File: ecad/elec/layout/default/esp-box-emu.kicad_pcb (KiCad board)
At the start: 2 copper layers, 225.7 x 100.8 mm, 0 parts

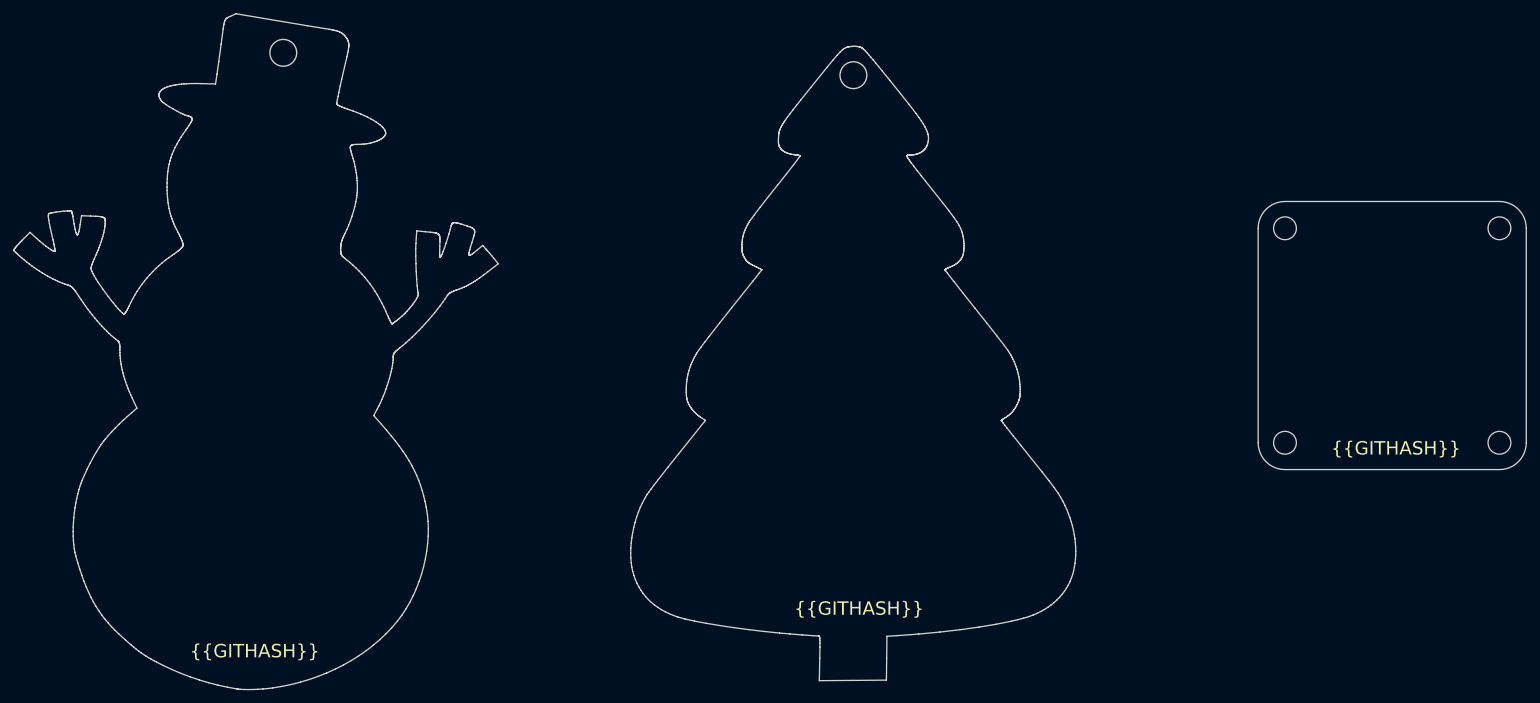
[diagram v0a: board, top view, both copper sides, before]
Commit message: wip: fleshing out ecad in atopile for fun
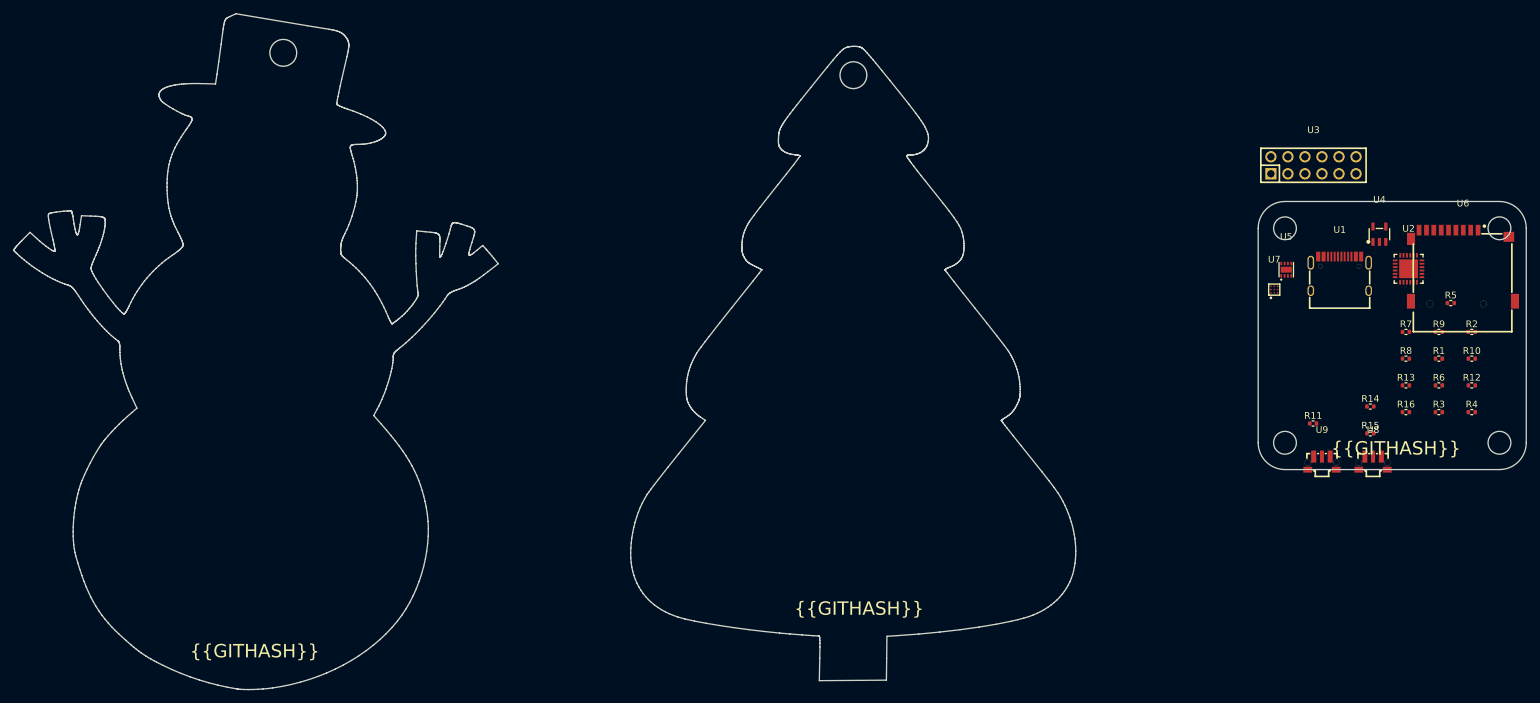
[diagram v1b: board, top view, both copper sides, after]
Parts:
- added R1: 62.5mW Thick Film Resistors ±100ppm/℃ ±1% 5.1kΩ 0402 Chip R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, lib:R0402, F.Cu at (248.6, 101.2)
- added R10: 62.5mW Thick Film Resistors ±100ppm/℃ ±1% 10kΩ 0402 Chip Re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, lib:R0402, F.Cu at (253.5, 101.2)
- added R11: 62.5mW Thick Film Resistors ±100ppm/℃ ±1% 10kΩ 0402 Chip Re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, lib:R0402, F.Cu at (229.8, 110.9)
- added R12: 62.5mW Thick Film Resistors ±100ppm/℃ ±1% 10kΩ 0402 Chip Re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, lib:R0402, F.Cu at (253.5, 105.2)
- added R13: 62.5mW Thick Film Resistors ±100ppm/℃ ±1% 10kΩ 0402 Chip Re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, lib:R0402, F.Cu at (243.7, 105.2)
- added R14: 62.5mW Thick Film Resistors ±100ppm/℃ ±1% 10kΩ 0402 Chip Re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, lib:R0402, F.Cu at (238.4, 108.4)
- added R15: 62.5mW Thick Film Resistors ±100ppm/℃ ±1% 10kΩ 0402 Chip Re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, lib:R0402, F.Cu at (238.4, 112.4)
- added R16: 62.5mW Thick Film Resistors ±100ppm/℃ ±1% 10kΩ 0402 Chip Re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, lib:R0402, F.Cu at (243.7, 109.2)
- added R2: 62.5mW Thick Film Resistors ±100ppm/℃ ±1% 5.1kΩ 0402 Chip R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, lib:R0402, F.Cu at (253.5, 97.2)
- added R3: 62.5mW Thick Film Resistors ±100ppm/℃ ±1% 10kΩ 0402 Chip Re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, lib:R0402, F.Cu at (248.6, 109.2)
- added R4: 62.5mW Thick Film Resistors ±100ppm/℃ ±1% 10kΩ 0402 Chip Re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, lib:R0402, F.Cu at (253.5, 109.2)
- added R5: 62.5mW Thick Film Resistors ±100ppm/℃ ±1% 10kΩ 0402 Chip Re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, lib:R0402, F.Cu at (250.4, 93.0)
- added R6: 62.5mW Thick Film Resistors ±100ppm/℃ ±1% 10kΩ 0402 Chip Re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, lib:R0402, F.Cu at (248.6, 105.2)
- added R7: 62.5mW Thick Film Resistors ±100ppm/℃ ±1% 10kΩ 0402 Chip Re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, lib:R0402, F.Cu at (243.7, 97.2)
- added R8: 62.5mW Thick Film Resistors ±100ppm/℃ ±1% 10kΩ 0402 Chip Re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, lib:R0402, F.Cu at (243.7, 101.2)
- added R9: 62.5mW Thick Film Resistors ±100ppm/℃ ±1% 10kΩ 0402 Chip Re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, lib:R0402, F.Cu at (248.6, 97.2)
- added U1: , lib:USB-C-SMD_TYPE-611-T3-W, F.Cu at (233.8, 88.6)
- added U2: , lib:VFQFPN-24_L4.0-W4.0-P0.50-BL-EP2.8, F.Cu at (244.1, 87.8)
- added U3: , lib:HDR-TH_12P-P2.54-V-M-R2-C6-S2.54, F.Cu at (229.9, 72.4)
- added U4: , lib:SOT-23-5_L3.0-W1.7-P0.95-LS2.8-BL, F.Cu at (239.7, 82.7)
- added U5: , lib:DFN-8_L2.0-W2.0-P0.50-BL-EP, F.Cu at (225.8, 88.0)
- added U6: , lib:SIM-SMD_C9900007362, F.Cu at (252.2, 87.4)
- added U7: , lib:DSBGA-9_L1.5-W1.5-R3-C3-P0.50-BL, F.Cu at (224.0, 90.9)
- added U8: , lib:SW-SMD_E-SWITCH_TL3340, F.Cu at (238.8, 116.8)
- added U9: , lib:SW-SMD_E-SWITCH_TL3340, F.Cu at (231.1, 116.8)
